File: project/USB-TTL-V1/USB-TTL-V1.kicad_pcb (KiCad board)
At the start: 4 copper layers, 31 x 11.3 mm, 22 parts, among them J1 TTL, J2 usbc, Q1 q1, Q2 q2, U1 CH340C, U2 SPX3819M5-L-3-3

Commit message: feat: power bank
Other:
- board text added: "3.3"
- board text added: "GND"
- board text added: "GPIO0"
- board text added: "RST"
- board text added: "RXD"
- board text added: "TXD"
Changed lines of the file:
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@@
     (property "Sheetname" "")
     (attr smd)
-    (fp_text reference "R4" (at 0.07 0.88 270) (layer "F.SilkS")
+    (fp_text reference "R4" (at -0.04 -0.82 270) (layer "F.SilkS")
       (effects (font (size 0.6 0.6) (thickness 0.05)))
     )
@@
     (property "Sheetname" "")
     (attr smd)
-    (fp_text reference "R3" (at 0.01 -0.99 -90) (layer "F.SilkS")
+    (fp_text reference "R3" (at -1.36 -1 -90) (layer "F.SilkS")
       (effects (font (size 0.6 0.6) (thickness 0.05)))
     )
@@
   )
   (gr_rect (start 102.33 81.57) (end 133.34 92.87) (layer "Edge.Cuts") (width 0.1) (fill none))
+  (gr_text "GND\n" (at 129.37 85.39 -180) (layer "B.SilkS")
+    (effects (font (size 0.8 0.8) (thickness 0.1)) (justify mirror))
+  )
+  (gr_text "3.3" (at 129.65 84.08 -180) (layer "B.SilkS")
+    (effects (font (size 0.8 0.8) (thickness 0.1)) (justify mirror))
+  )
+  (gr_text "RST\n" (at 129.56 86.77) (layer "B.SilkS")
+    (effects (font (size 0.8 0.8) (thickness 0.1)) (justify mirror))
+  )
+  (gr_text "TXD\n" (at 129.53 90.45 -180) (layer "B.SilkS")
+    (effects (font (size 0.8 0.8) (thickness 0.1)) (justify mirror))
+  )
+  (gr_text "GPIO0" (at 128.83 87.87 -180) (layer "B.SilkS")
+    (effects (font (size 0.8 0.8) (thickness 0.1)) (justify mirror))
+  )
+  (gr_text "RXD" (at 129.43 89.27 -180) (layer "B.SilkS")
+    (effects (font (size 0.8 0.8) (thickness 0.1)) (justify mirror))
+  )
   (segment (start 124.95 83.861428) (end 124.95 82.51) (width 0.4) (layer "F.Cu") (net 1))
   (segment (start 111.579022 90.54) (end 110.555 90.54) (width 0.4) (layer "F.Cu") (net 1))

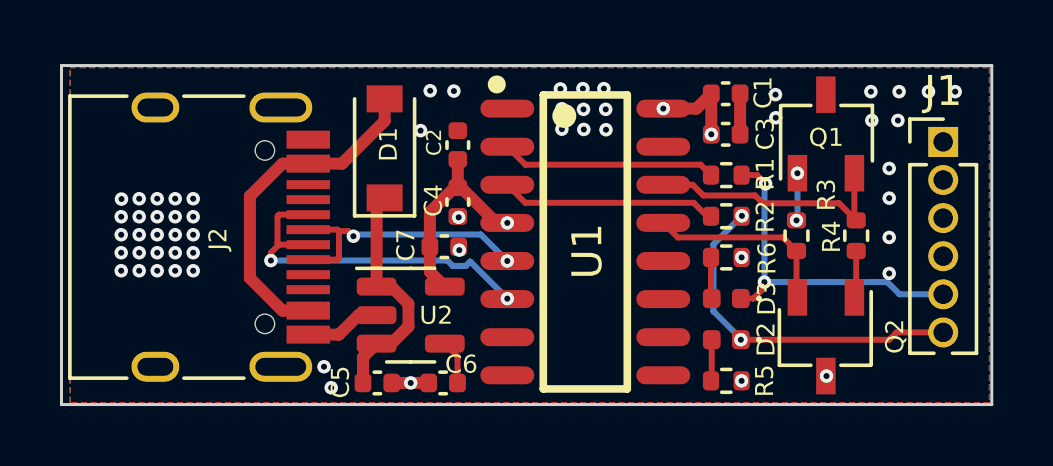
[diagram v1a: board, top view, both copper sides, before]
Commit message: fix: screen rst and cs
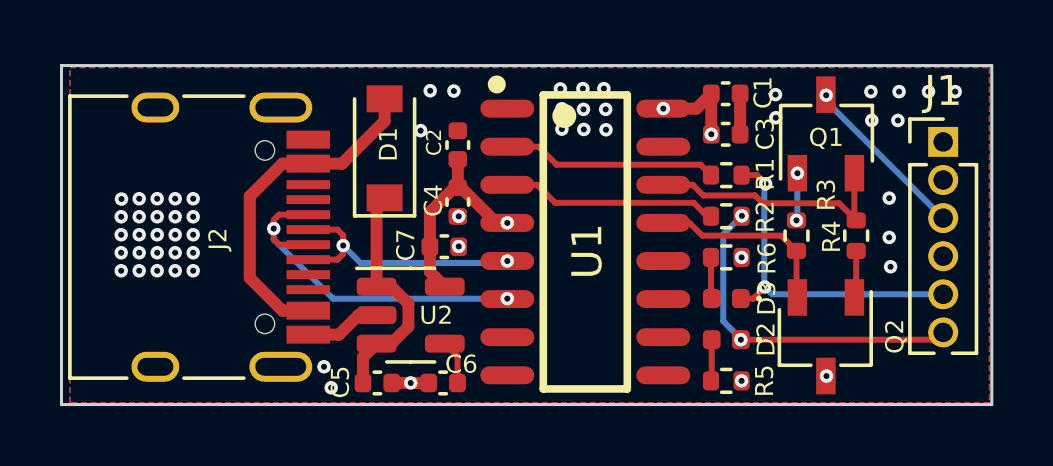
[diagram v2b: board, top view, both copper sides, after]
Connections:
- Q1 pad 3: /nRST -> /RST
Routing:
- net /RST: track 0.00 -> 5.74 mm, vias 0 -> 1
- net GND: track 5.33 -> 5.32 mm, vias 54 -> 53

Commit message: feat: update usb - ttl
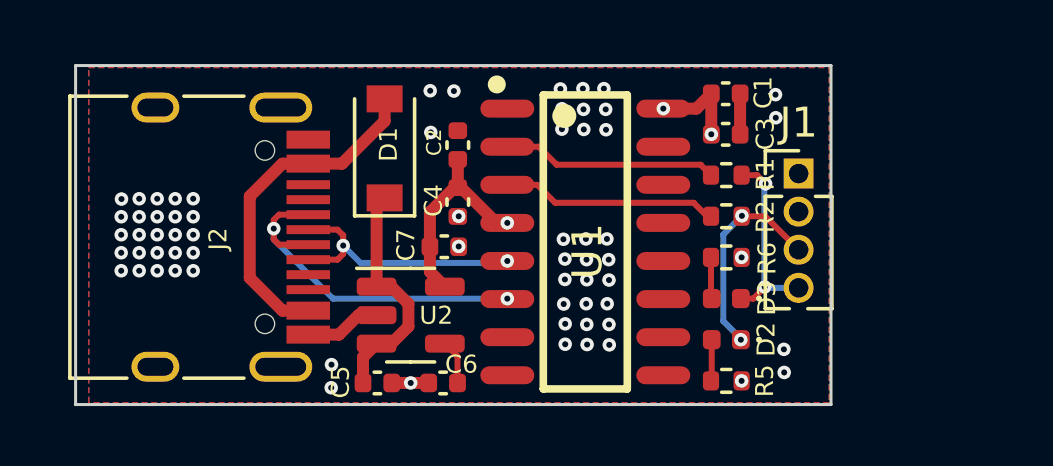
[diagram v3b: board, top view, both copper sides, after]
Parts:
- removed Q1: q1, Package_TO_SOT_SMD:TSOT-23
- removed Q2: q2, Package_TO_SOT_SMD:TSOT-23
- removed R3, R4: 12K, Resistor_SMD:R_0402_1005Metric
- J1: value TTL -> TTL-connect-pin4; footprint Connector_PinHeader_1.27mm:PinHeader_1x06_P1.27mm_Vertical -> Connector_PinHeader_1.27mm:PinHeader_1x04_P1.27mm_Vertical
- moved J1 4.93 mm to (126.9, 85.2)
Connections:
- J1 pad 1: +3V3 -> GND
- J1 pad 3: /RST -> /TXD
- J1 pad 4: /GPIO0 -> /RXD
- U1 pad 13: Net-(Q2-Pad2) -> unconnected-(U1-Pad13)
- U1 pad 14: Net-(Q1-Pad2) -> unconnected-(U1-Pad14)
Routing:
- net Net-(Q1-Pad2): track 8.52 -> 0.00 mm
- net +3V3: track 33.9 -> 26.1 mm
- net Net-(Q2-Pad2): track 6.39 -> 0.00 mm
- net /RST: track 5.74 -> 0.00 mm, vias 1 -> 0
- net /GPIO0: track 5.63 -> 0.00 mm, vias 1 -> 0
- net /RXD: track 11.4 -> 6.48 mm
- net /TXD: track 11.5 -> 7.01 mm
- net Net-(Q1-Pad1): track 1.58 -> 0.00 mm, vias 2 -> 0
- net Net-(Q2-Pad1): track 1.57 -> 0.00 mm
- net GND: vias 53 -> 64
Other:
- board size 31 x 11.3 mm -> 25.2 x 11.3 mm
- board text removed: "3.3"
- board text removed: "RST"

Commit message: fix: update screen  usb-ttl
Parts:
- removed C4, C7: 10uf, Capacitor_SMD:C_0402_1005Metric
- removed C5: 1uf, Capacitor_SMD:C_0402_1005Metric
- removed C6: 470pf, Capacitor_SMD:C_0402_1005Metric
- removed D1: B120-E3, Diode_SMD:D_SOD-123
- removed U2: SPX3819M5-L-3-3, Package_TO_SOT_SMD:SOT-23-5
- added Q1: S8050, Package_TO_SOT_SMD:TSOT-23, F.Cu at (122.7, 90.5)
- added Q2: S8050, Package_TO_SOT_SMD:TSOT-23, F.Cu at (122.7, 84.2)
- added R3: 12K, Resistor_SMD:R_0402_1005Metric, F.Cu at (123.6, 87.3)
- added R4: 12K, Resistor_SMD:R_0402_1005Metric, F.Cu at (121.7, 87.3)
- J1: footprint Connector_PinHeader_1.27mm:PinHeader_1x04_P1.27mm_Vertical -> Connector_PinHeader_2.00mm:PinHeader_1x05_P2.00mm_Vertical
- R5, R6: value 1k -> 4.7k
- moved C3 9.45 mm to (119.9, 92.2)
- moved R2 6.29 mm to (120.0, 90.9)
- moved R5 5.78 mm to (120.0, 88.5)
- moved D3 5.59 mm to (120.0, 86.1)
- moved D2 4.65 mm to (120.0, 89.7)
- moved R6 4.59 mm to (120.0, 87.3)
- moved R1 4.55 mm to (120.0, 84.9)
- moved C1 4.54 mm to (119.9, 82.4)
- moved C2 4.43 mm to (119.9, 83.6), turned to 0 degrees
- moved U1 4.39 mm to (115.4, 87.4)
- moved J1 2.58 mm to (125.2, 83.2)
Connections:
- C1 pad 1: +3V3 -> +5V
- C2 pad 1: +3V3 -> +5V
- C3 pad 1: +3V3 -> Net-(C3-Pad1)
- J1 pad 2: GND -> /GPIO0
- J1 pad 3: /TXD -> /RXD
- J1 pad 4: /RXD -> /TXD
- J2 pad A4: Net-(D1-Pad2) -> +5V
- J2 pad A9: Net-(D1-Pad2) -> +5V
- J2 pad B4: Net-(D1-Pad2) -> +5V
- J2 pad B9: Net-(D1-Pad2) -> +5V
- R5 pad 1: +3V3 -> +5V
- R6 pad 1: +3V3 -> +5V
- U1 pad 13: unconnected-(U1-Pad13) -> Net-(Q2-Pad2)
- U1 pad 14: unconnected-(U1-Pad14) -> Net-(Q1-Pad2)
- U1 pad 16: +3V3 -> +5V
- U1 pad 4: +3V3 -> Net-(C3-Pad1)
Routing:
- net +3V3: track 26.1 -> 0.00 mm, vias 5 -> 0
- net +5V: track 0.00 -> 13.4 mm, vias 0 -> 9
- net Net-(D1-Pad2): track 11.4 -> 0.00 mm
- net Net-(Q1-Pad2): track 0.00 -> 9.98 mm, vias 0 -> 2
- net Net-(C3-Pad1): track 0.00 -> 8.79 mm, vias 0 -> 2
- net +5VD: track 7.92 -> 0.00 mm
- net Net-(Q2-Pad2): track 0.00 -> 6.94 mm, vias 0 -> 2
- net GND: track 5.32 -> 0.00 mm, vias 64 -> 0
- net Net-(J2-PadA7): track 12.1 -> 6.95 mm
- net Net-(J2-PadA6): track 8.84 -> 4.45 mm, vias 2 -> 0
- net /GPIO0: track 0.00 -> 3.53 mm
- net /EN: track 0.00 -> 2.73 mm
- net Net-(R2-Pad1): track 7.22 -> 8.90 mm, vias 0 -> 2
- net Net-(C6-Pad1): track 1.49 -> 0.00 mm
- net Net-(Q2-Pad1): track 0.00 -> 1.33 mm
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- added copper zone on In1.Cu, net +5V
- removed copper zone on In1.Cu, net GND
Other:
- board size 25.2 x 11.3 mm -> 23.9 x 11.3 mm
- board text added: "EN"

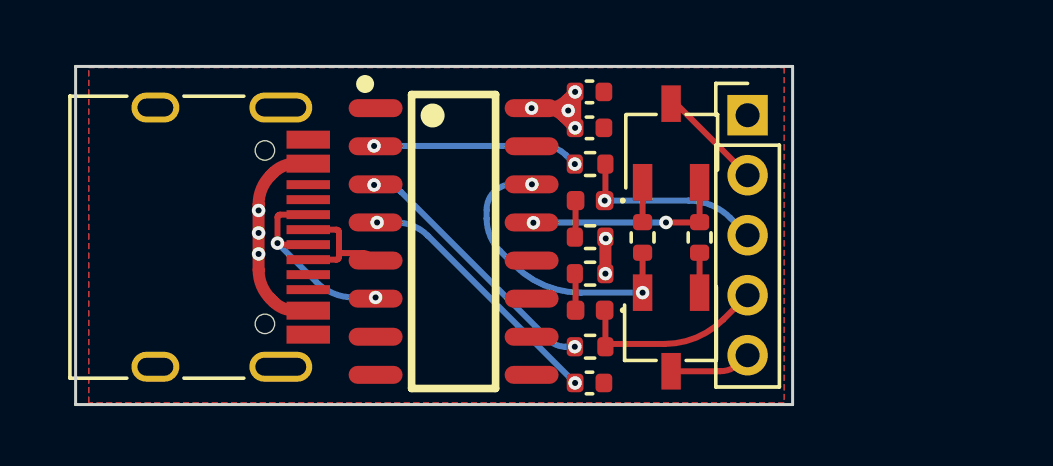
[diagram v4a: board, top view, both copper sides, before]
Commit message: update plant carer 1.2
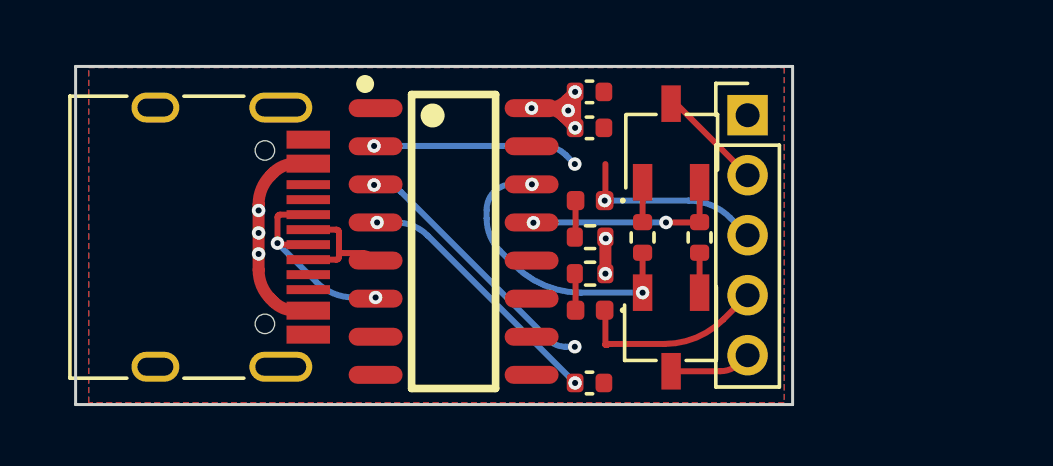
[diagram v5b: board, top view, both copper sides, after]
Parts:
- removed R1, R2: 470, Resistor_SMD:R_0402_1005Metric
- R5, R6: value 4.7k -> 12K
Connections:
- U1 pad 2: Net-(R1-Pad2) -> /RXD
- U1 pad 3: Net-(R2-Pad1) -> /TXD
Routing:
- net /TXD: track 6.62 -> 15.5 mm, vias 0 -> 2
- net Net-(R2-Pad1): track 8.90 -> 0.00 mm, vias 2 -> 0
- net Net-(R1-Pad2): track 6.94 -> 0.00 mm, vias 2 -> 0
- net /RXD: track 6.37 -> 13.3 mm, vias 1 -> 3
